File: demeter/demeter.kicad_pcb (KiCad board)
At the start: 2 copper layers, 116.2 x 107.4 mm, 23 parts, among them SW10 SW_Push, SW11 SW_Push, SW12 SW_Push, SW14 SW_Push, SW15 SW_Push, SW16 SW_Push, SW17 SW_Push, SW18 SW_Push, SW2 SW_Push, SW2 SW_SPDT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

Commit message: update legend
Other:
- board text added: "Demeter v0.2.yy"
- board text removed: "12:45"
- board text removed: "Demeter v0.2"
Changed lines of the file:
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@@
 		(layer "Edge.Cuts")
 	)
-	(gr_text "Demeter v0.2"
+	(gr_text "Demeter v0.2.yy"
 		(at 131.59 52.09 0)
 		(layer "F.SilkS")
@@
 			)
 			(justify left bottom)
-		)
-	)
-	(gr_text "12:45"
-		(at 114.88 48.33 0)
-		(layer "F.SilkS")
-		(effects
-			(font
-				(size 1 1)
-				(thickness 0.15)
-			)
-			(justify left bottom)

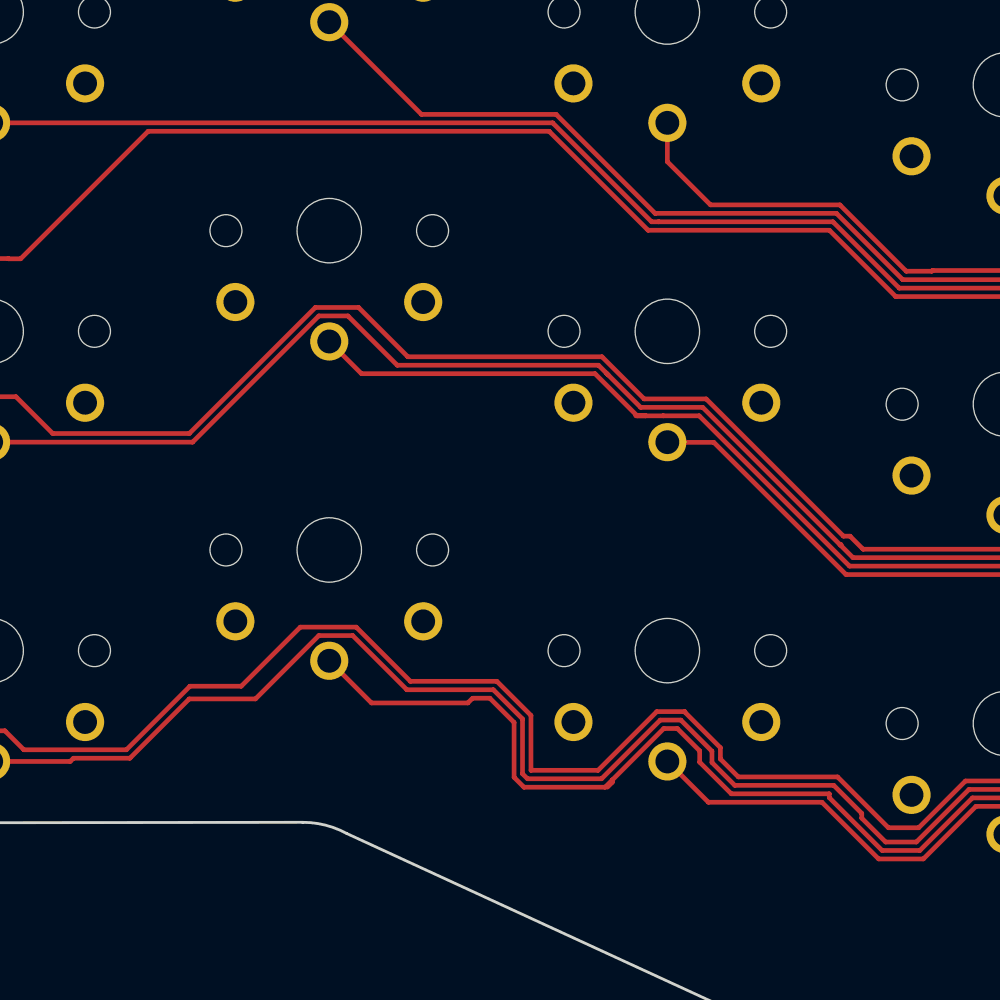
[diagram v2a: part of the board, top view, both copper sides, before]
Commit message: add modified tenting puck footprint
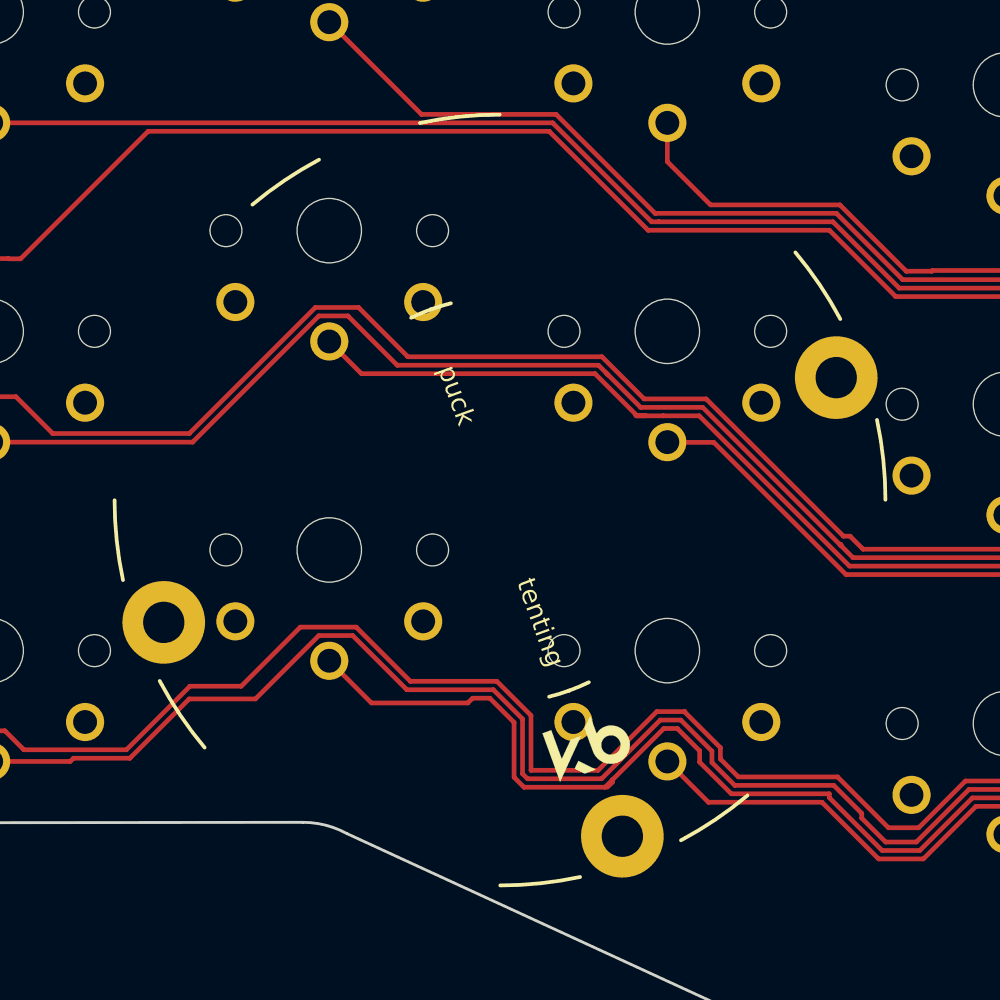
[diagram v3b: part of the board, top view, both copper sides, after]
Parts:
- added REF**: Tenting Puck, TentingPuck:TentingPuck three hole, F.Cu at (131.0, 85.0)

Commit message: add monkey image
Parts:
- added G***: LOGO, Images:monkey silkscreen, B.Cu at (147.0, 108.0)
